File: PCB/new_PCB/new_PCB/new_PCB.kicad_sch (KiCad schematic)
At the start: 10 parts, among them J1 XT60PW-F, U1 ESP32-S3-DEVKITC-1-N16R8V

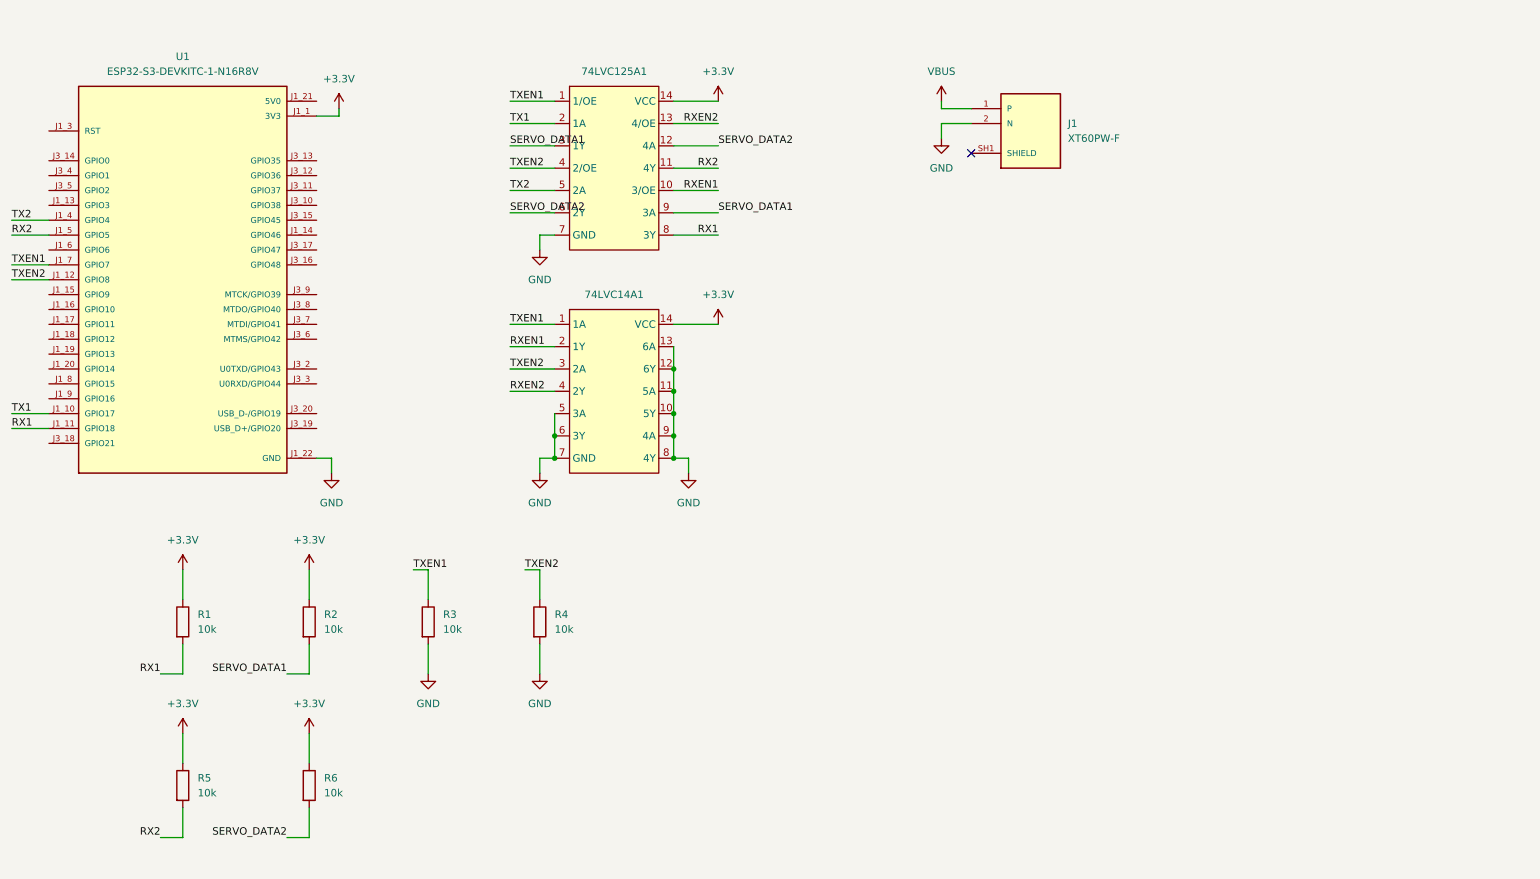
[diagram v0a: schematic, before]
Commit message: Add servo connectors and 3d models
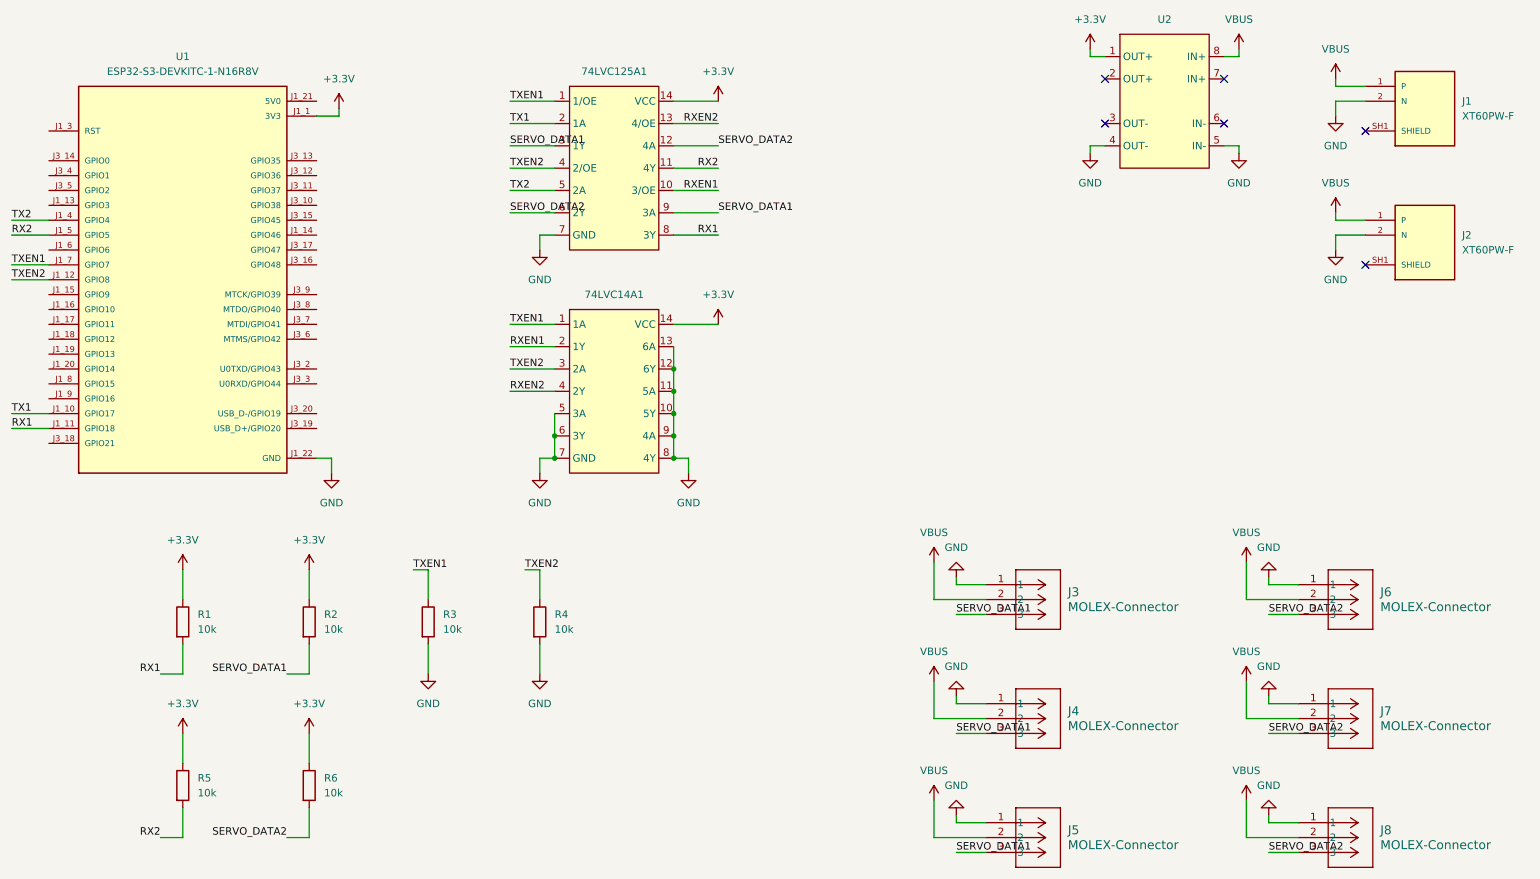
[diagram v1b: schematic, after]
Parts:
- added J2: XT60PW-F, Elements:AMASS-XT60PW-F, symbol Elements:XT60PW-F
- added J3, J4, J5, J6, J7, J8: MOLEX-Connector, CONN_22035035_MOL, symbol Elements:MOLEX-Connector
- added U2: (no value), Elements:MP1584EN, symbol Elements:MP1584EN
- J1: footprint XT60PW-F:AMASS_XT60PW-F -> Elements:AMASS-XT60PW-F
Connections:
- net +3.3V: now also U2.1 (OUT+)
- net GND: now also J2.2 (N), J3.1, J4.1, J5.1, J6.1, J7.1, J8.1, U2.4 (OUT-), U2.5 (IN-)
- net SERVO_DATA1: now also J3.3, J4.3, J5.3
- net SERVO_DATA2: now also J6.3, J7.3, J8.3
- net VBUS: now also J2.1 (P), J3.2, J4.2, J5.2, J6.2, J7.2, J8.2, U2.8 (IN+)
- new net: J2.SH1 (SHIELD), J2.SH2 (SHIELD)
- no-connect marks 1 -> 6
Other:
- moved on the sheet: J1

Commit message: Add first quick version of PCB routing
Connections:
- net RX1: now also 74LVC125A1.6 (2Y); no longer 74LVC125A1.8 (3Y)
- net RXEN1: now also 74LVC125A1.4 (2/OE), 74LVC14A1.4 (2Y); no longer 74LVC125A1.10 (3/OE), 74LVC14A1.2 (1Y)
- net RXEN2: now also 74LVC14A1.2 (1Y); no longer 74LVC14A1.4 (2Y)
- net SERVO_DATA1: now also 74LVC125A1.5 (2A); no longer 74LVC125A1.9 (3A)
- net SERVO_DATA2: now also 74LVC125A1.8 (3Y); no longer 74LVC125A1.6 (2Y)
- net TX2: now also 74LVC125A1.9 (3A); no longer 74LVC125A1.5 (2A)
- net TXEN1: now also 74LVC14A1.3 (2A); no longer 74LVC14A1.1 (1A)
- net TXEN2: now also 74LVC125A1.10 (3/OE), 74LVC14A1.1 (1A); no longer 74LVC125A1.4 (2/OE), 74LVC14A1.3 (2A)
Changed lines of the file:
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@@
 		)
 	)
-	(label "RXEN1"
+	(label "TXEN2"
 		(at 146.05 45.72 180)
 		(effects
@@
 		)
 	)
+	(label "RXEN1"
+		(at 110.49 80.01 0)
+		(effects
+			(font
+				(size 1.27 1.27)
+			)
+			(justify left bottom)
+		)
+	)
+	(label "RX1"
+		(at 110.49 49.53 0)
+		(effects
+			(font
+				(size 1.27 1.27)
+			)
+			(justify left bottom)
+		)
+	)
 	(label "RXEN2"
-		(at 110.49 80.01 0)
-		(effects
-			(font
-				(size 1.27 1.27)
-			)
-			(justify left bottom)
-		)
-	)
-	(label "SERVO_DATA2"
-		(at 110.49 49.53 0)
-		(effects
-			(font
-				(size 1.27 1.27)
-			)
-			(justify bottom)
-		)
-	)
-	(label "RXEN1"
 		(at 110.49 72.39 0)
 		(effects
@@
 		)
 	)
-	(label "SERVO_DATA1"
-		(at 146.05 49.53 0)
-		(effects
-			(font
-				(size 1.27 1.27)
-			)
-			(justify bottom)
+	(label "TX2"
+		(at 146.05 49.53 180)
+		(effects
+			(font
+				(size 1.27 1.27)
+			)
+			(justify right bottom)
 		)
 	)
@@
 		)
 	)
-	(label "TXEN2"
+	(label "TXEN1"
 		(at 110.49 76.2 0)
 		(effects
@@
 		)
 	)
-	(label "RX1"
-		(at 146.05 53.34 180)
-		(effects
-			(font
-				(size 1.27 1.27)
-			)
-			(justify right bottom)
+	(label "SERVO_DATA2"
+		(at 146.05 53.34 0)
+		(effects
+			(font
+				(size 1.27 1.27)
+			)
+			(justify bottom)
 		)
 	)
@@
 		)
 	)
-	(label "TX2"
+	(label "SERVO_DATA1"
 		(at 110.49 45.72 0)
 		(effects
@@
 				(size 1.27 1.27)
 			)
-			(justify left bottom)
-		)
-	)
-	(label "TXEN1"
+			(justify bottom)
+		)
+	)
+	(label "TXEN2"
 		(at 110.49 68.58 0)
 		(effects
@@
 		)
 	)
-	(label "TXEN2"
+	(label "RXEN1"
 		(at 110.49 41.91 0)
 		(effects
